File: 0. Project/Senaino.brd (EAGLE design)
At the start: 68.6 x 53.3 mm, 37 parts, among them Q1 16 MHz, Q2 12 MHz, U1 ATMEGA328P-PU, U3 7805T, U4 CH340G

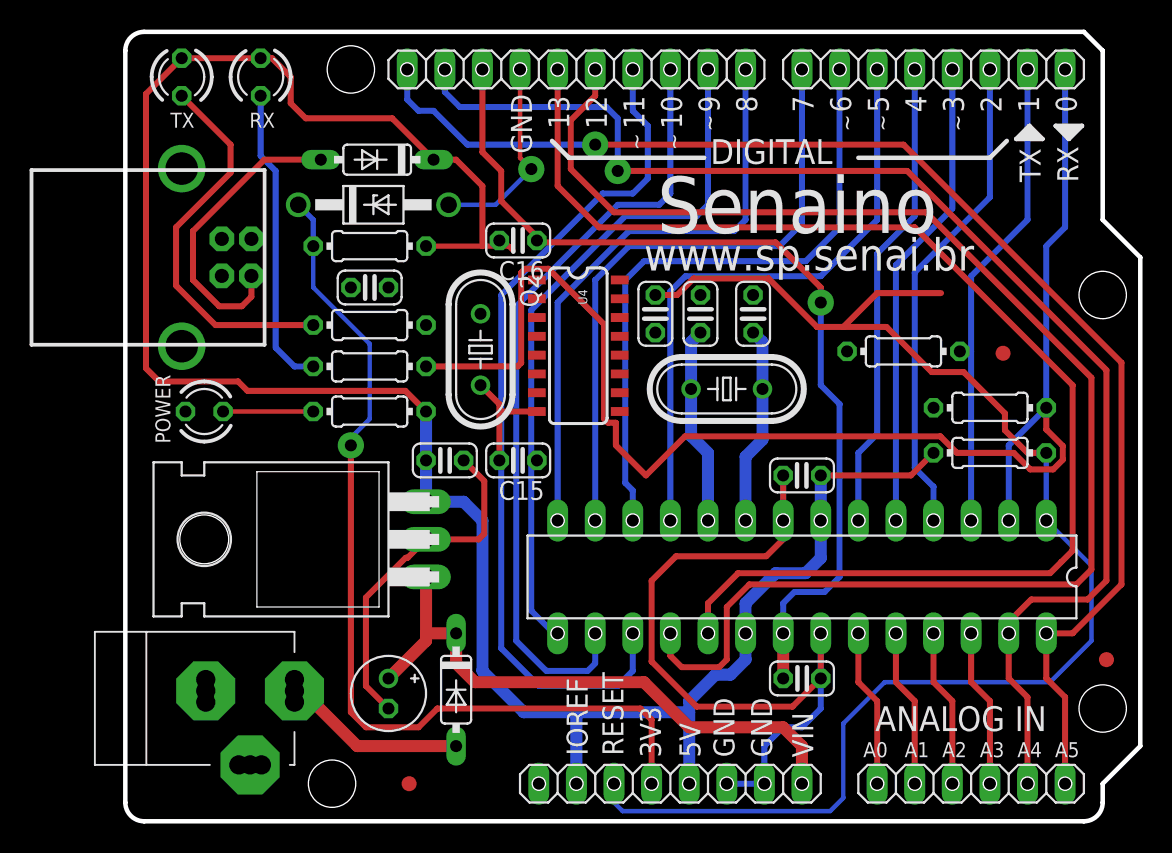
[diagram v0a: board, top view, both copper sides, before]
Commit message: Changes to CH340 performed
- Schematic OK.
- Layout OK.
- BOM OK.
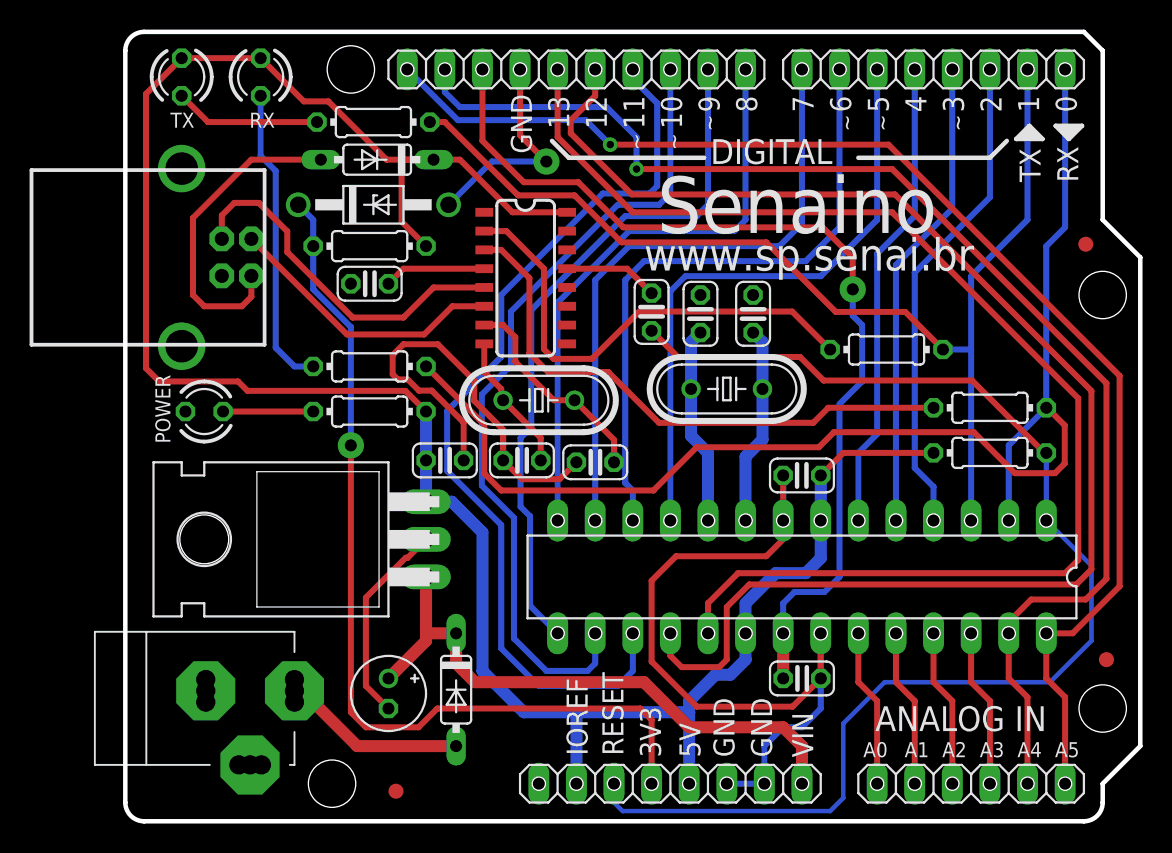
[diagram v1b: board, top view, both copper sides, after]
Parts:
- moved C16 15.9 mm to (31.8, 24.3), turned to 0 degrees
- moved R4 13.7 mm to (16.8, 47.2)
- moved FD1 9.25 mm to (64.9, 39.0), turned to 0 degrees
- moved U4 5.79 mm to (27.1, 36.7)
- moved Q2 5.22 mm to (27.9, 28.4), turned to 180 degrees
- moved R6 1.15 mm to (51.4, 31.9)
- moved FD3 1.02 mm to (18.3, 2.03)
- moved C3 0.28 mm to (35.6, 34.4), turned to 90 degrees
- moved C4 0.25 mm to (16.5, 36.3)
- moved C15 0.25 mm to (26.8, 24.4), turned to 0 degrees
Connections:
- net GND: now also C15.1, C16.1
- net PE: no longer C15.1, C16.1
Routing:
- net D1: track 32.1 -> 75.0 mm
- net N$10: track 0.00 -> 38.6 mm
- net N$4: track 0.00 -> 32.5 mm
- net N$2: track 0.00 -> 24.5 mm
- net GND: track 91.0 -> 113.6 mm
- net N$5: track 0.00 -> 19.2 mm
- net N$9: track 26.1 -> 9.88 mm
- net N$13: track 0.00 -> 14.6 mm
- net D0: track 98.1 -> 88.0 mm
- net RESET: track 95.4 -> 85.5 mm
- net N$11: track 0.00 -> 6.89 mm
- net N$3: track 0.00 -> 6.39 mm
- net D11: track 57.7 -> 62.0 mm
- net +5V: track 152.2 -> 155.8 mm
- net AREF: track 63.1 -> 65.2 mm
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
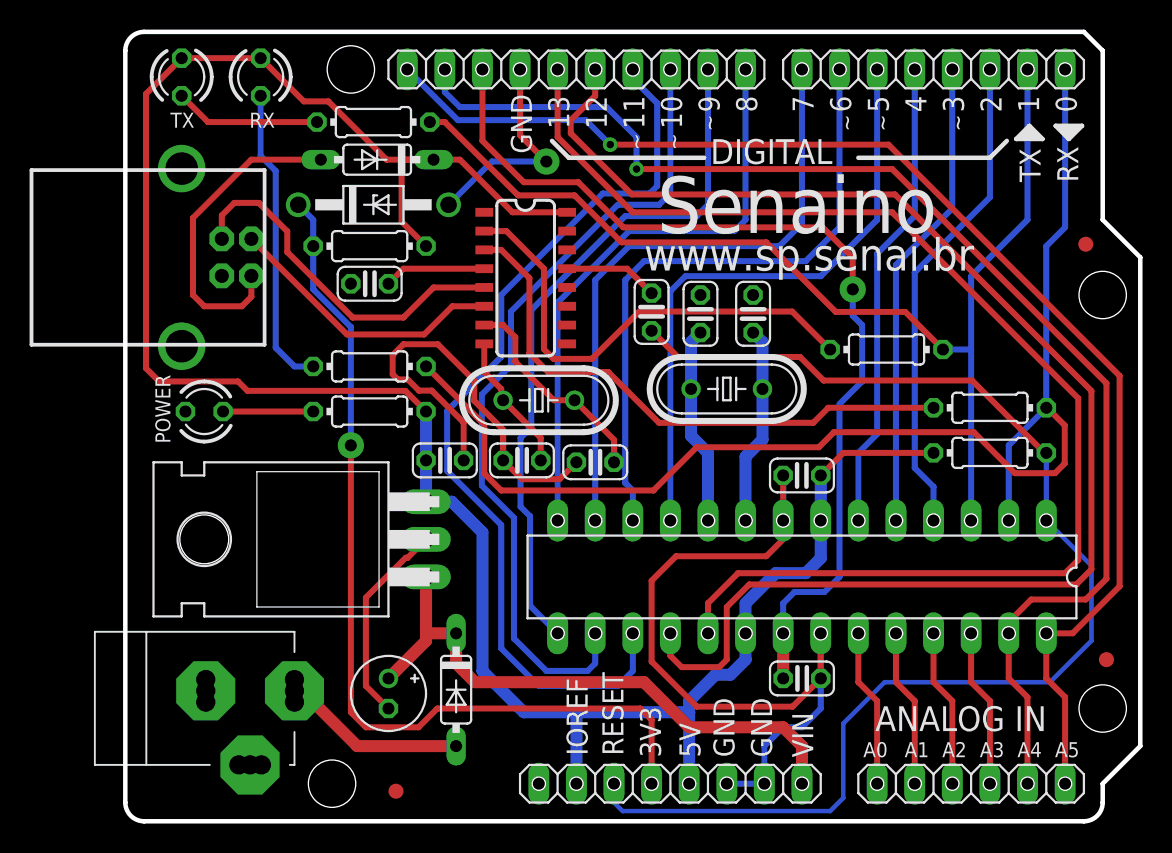
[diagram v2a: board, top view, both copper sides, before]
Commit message: pin 1 from CH340 added to GND & R3/R4 changed to 1k
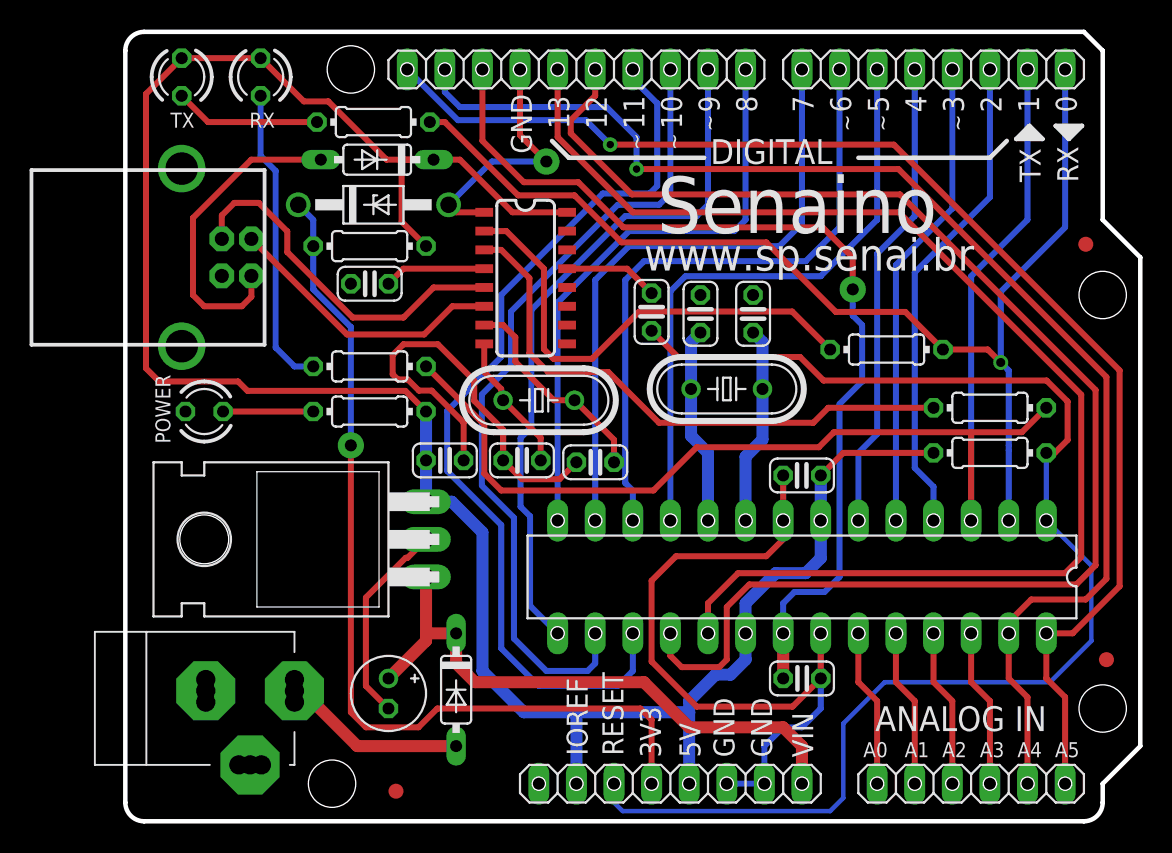
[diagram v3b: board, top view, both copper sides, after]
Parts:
- R3, R4: value 330R -> 1k
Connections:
- removed net PE: U4.1
- net D0: now also R4.1, R6.2; no longer R3.1, R7.2
- net D1: now also R3.1, R7.2; no longer R4.1, R6.2
- net GND: now also U4.1
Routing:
- net D1: track 75.0 -> 87.7 mm
- net D0: track 88.0 -> 77.8 mm, vias 0 -> 1
- net RESET: track 85.5 -> 89.9 mm
- net GND: track 113.6 -> 116.2 mm
